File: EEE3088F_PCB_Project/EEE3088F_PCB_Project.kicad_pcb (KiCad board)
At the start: 2 copper layers, 82 x 72.7 mm, 107 parts, among them IC1 DRV8833PWPR, IC2 DRV8833PWPR, IC3 TPS62067DSGR, IC5 INA219AIDCNR, IC7 TPS61088RHLR, J1 Conn_02x16_Odd_Even, J2 TYPE-C16PIN, J3 Conn_01x02, Q1 AO3400A, Q2 AO3400A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

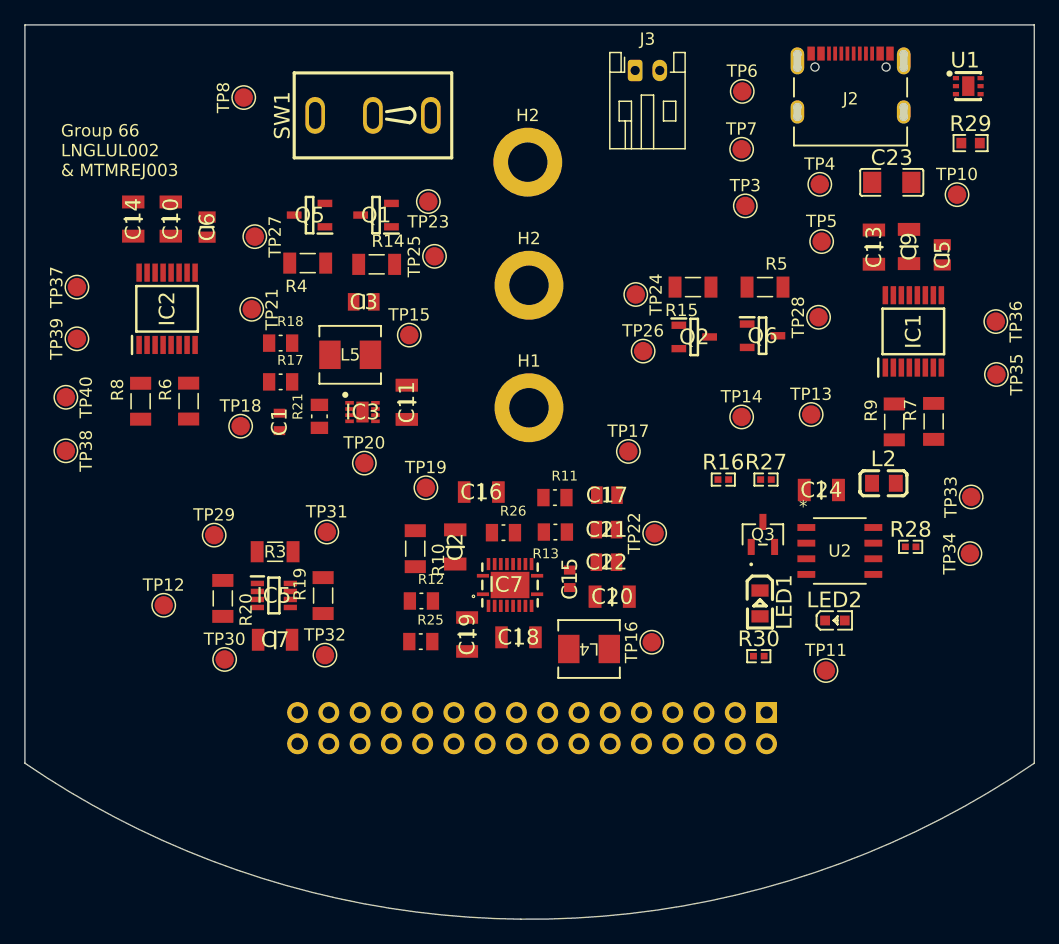
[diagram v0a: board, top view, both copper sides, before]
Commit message: v1.5.1
- tried adding wiring but hit edge
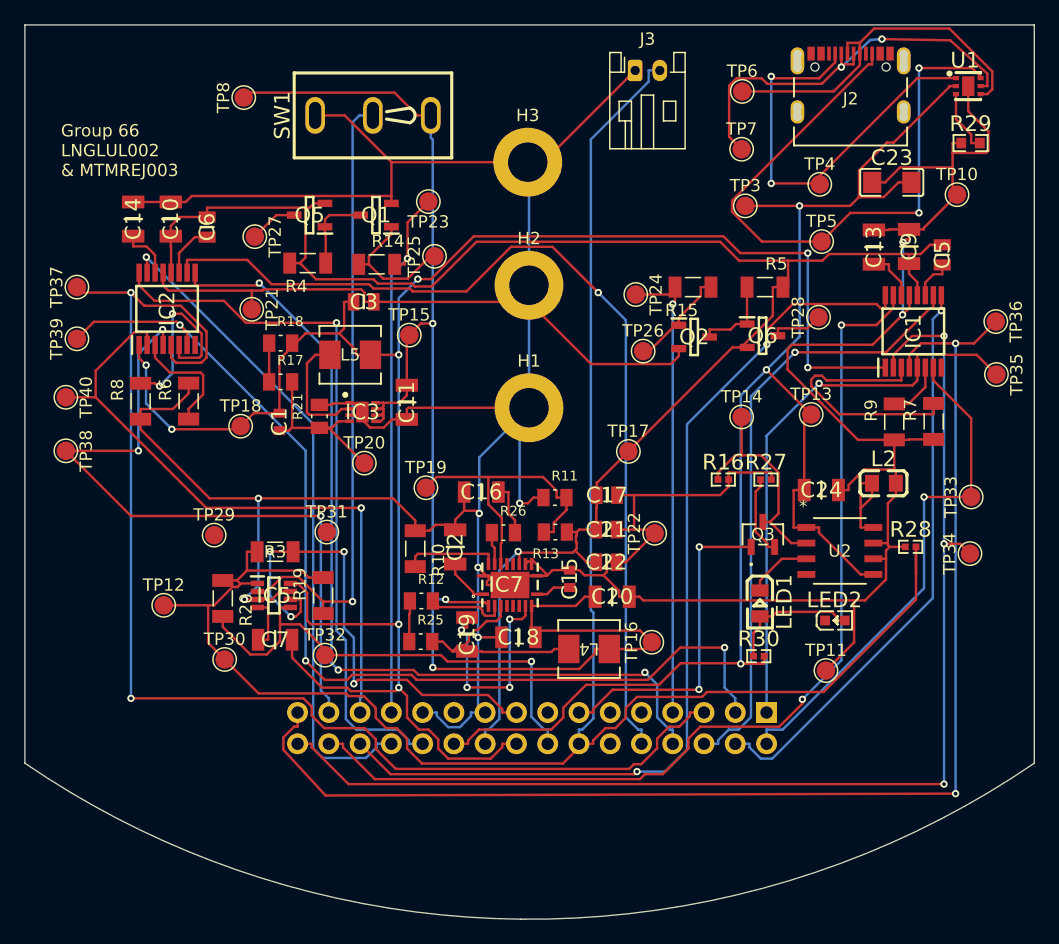
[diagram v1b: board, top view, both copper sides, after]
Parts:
- renumbered H2 to H3
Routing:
- net GND: track 0.00 -> 405.5 mm, vias 0 -> 8
- net /3V3 OUT: track 0.00 -> 157.0 mm, vias 0 -> 8
- net /BATTERY: track 0.00 -> 156.5 mm
- net /5V OUT: track 0.00 -> 141.1 mm, vias 0 -> 1
- net /HV: track 0.00 -> 121.1 mm, vias 0 -> 3
- net /PWR SWITCH OUT: track 0.00 -> 116.3 mm, vias 0 -> 3
- net /MOTOR1_B_OUT: track 0.00 -> 105.7 mm, vias 0 -> 2
- net /MOTOR4_B_OUT: track 0.00 -> 103.7 mm, vias 0 -> 2
- net /MOTOR1_A_OUT: track 0.00 -> 98.7 mm, vias 0 -> 3
- net /MOTOR4_A_OUT: track 0.00 -> 84.2 mm, vias 0 -> 3
- net /MOTOR1_CTRL2: track 0.00 -> 80.7 mm, vias 0 -> 2
- net /MOTOR1_CTRL1: track 0.00 -> 76.9 mm, vias 0 -> 2
- net /MOTOR4_CTRL2: track 0.00 -> 76.8 mm, vias 0 -> 1
- net /MOTOR4_CTRL1: track 0.00 -> 72.5 mm, vias 0 -> 3
- net /MOTOR3_CTRL1: track 0.00 -> 58.1 mm, vias 0 -> 1
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
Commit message: Revert "v1.5.1"
This reverts commit 95b0540061ed2b4f31283696902dc0dbdf64c944.
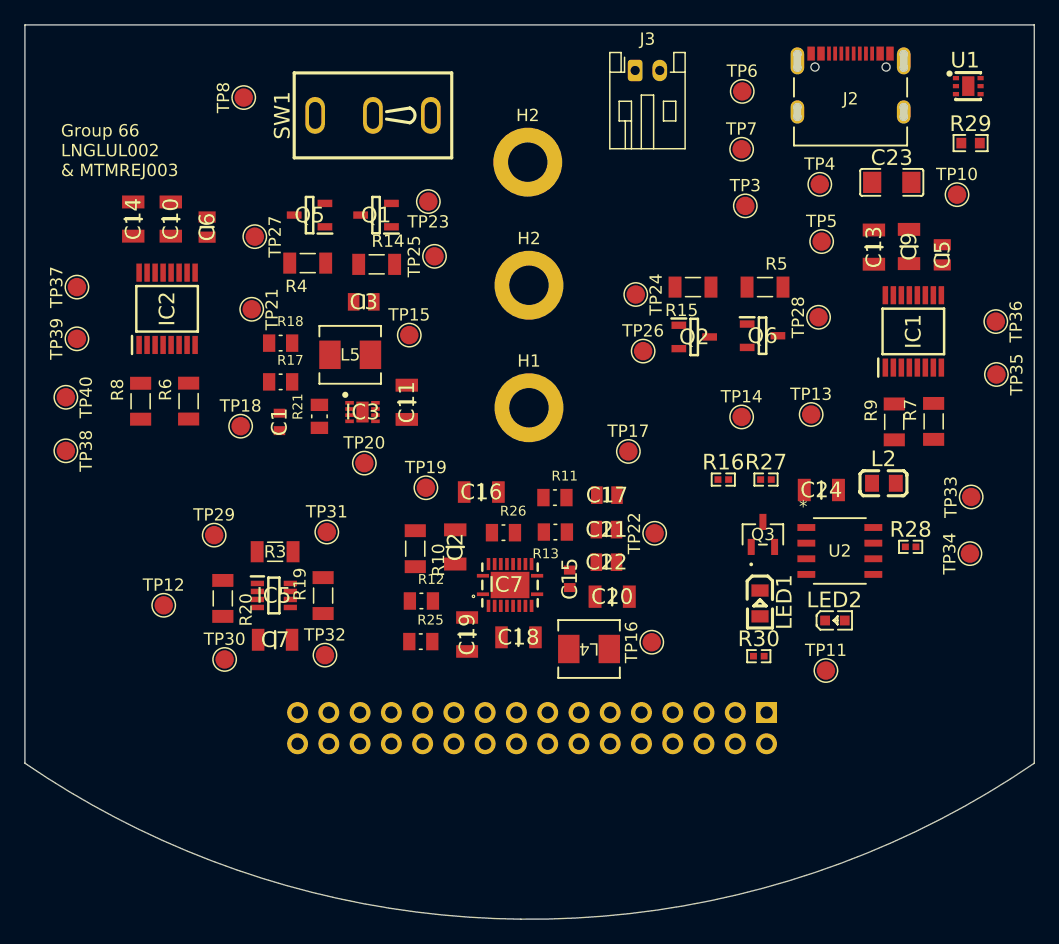
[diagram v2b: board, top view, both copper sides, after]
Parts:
- renumbered H3 to H2
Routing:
- net GND: track 405.5 -> 0.00 mm, vias 8 -> 0
- net /3V3 OUT: track 157.0 -> 0.00 mm, vias 8 -> 0
- net /BATTERY: track 156.5 -> 0.00 mm
- net /5V OUT: track 141.1 -> 0.00 mm, vias 1 -> 0
- net /HV: track 121.1 -> 0.00 mm, vias 3 -> 0
- net /PWR SWITCH OUT: track 116.3 -> 0.00 mm, vias 3 -> 0
- net /MOTOR1_B_OUT: track 105.7 -> 0.00 mm, vias 2 -> 0
- net /MOTOR4_B_OUT: track 103.7 -> 0.00 mm, vias 2 -> 0
- net /MOTOR1_A_OUT: track 98.7 -> 0.00 mm, vias 3 -> 0
- net /MOTOR4_A_OUT: track 84.2 -> 0.00 mm, vias 3 -> 0
- net /MOTOR1_CTRL2: track 80.7 -> 0.00 mm, vias 2 -> 0
- net /MOTOR1_CTRL1: track 76.9 -> 0.00 mm, vias 2 -> 0
- net /MOTOR4_CTRL2: track 76.8 -> 0.00 mm, vias 1 -> 0
- net /MOTOR4_CTRL1: track 72.5 -> 0.00 mm, vias 3 -> 0
- net /MOTOR3_CTRL1: track 58.1 -> 0.00 mm, vias 1 -> 0
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
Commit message: v1.5
- wiring done!
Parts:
- moved TP12 4.42 mm to (109.1, 95.2)
- moved TP31 4.42 mm to (122.3, 89.2)
- moved C7 4.42 mm to (118.2, 98.0)
- moved IC5 4.42 mm to (118.0, 94.4)
- moved R19 4.42 mm to (122.0, 94.4)
- moved R20 4.42 mm to (113.9, 94.6)
- moved R3 4.42 mm to (118.2, 90.8)
- moved TP29 4.42 mm to (113.2, 89.5)
- moved TP30 4.42 mm to (114.0, 99.6)
- moved TP32 4.42 mm to (122.2, 99.2)
- moved LED1 0.87 mm to (162.2, 97.3)
- moved LED2 0.87 mm to (168.3, 98.7)
- moved C24 0.87 mm to (167.2, 88.1)
- moved L2 0.87 mm to (172.3, 87.5)
- moved Q3 0.87 mm to (162.4, 91.7)
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- renumbered H2 to H3
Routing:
- net GND: track 0.00 -> 396.5 mm
- net /5V OUT: track 0.00 -> 151.6 mm
- net /PWR SWITCH OUT: track 0.00 -> 108.9 mm
- net /HV: track 0.00 -> 107.7 mm
- net /MOTOR1_B_OUT: track 0.00 -> 93.4 mm
- net /MOTOR1_CTRL1: track 0.00 -> 80.5 mm
- net /MOTOR3_B_OUT: track 0.00 -> 52.7 mm
- net /MOTOR3_A_OUT: track 0.00 -> 51.7 mm
- net /BATTERY: track 0.00 -> 50.5 mm
- net /MOTOR2_A_OUT: track 0.00 -> 41.0 mm
- net /CC1: track 0.00 -> 36.4 mm
- net /3V3 OUT: track 0.00 -> 32.3 mm
- net /I2C1_SDA: track 0.00 -> 31.4 mm
- net /D+: track 0.00 -> 27.7 mm
- net /FAST_CHARGE_CTRL: track 0.00 -> 23.6 mm
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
